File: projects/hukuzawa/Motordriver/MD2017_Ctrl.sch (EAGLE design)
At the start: 7 parts, among them IC1 PIC16F648, J1 3X2A, Q1 CERALOCK

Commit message: 回路図製作経過
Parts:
- added D1, D2, D3, D4: Z-DIODE, FP-21T for MITS:Z-DIODE
- added LED1: (no value), FP-21T for MITS:LED5MM
- added R1: (no value), rcl:R-US_R3216W
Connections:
- new net A: IC1.RB5, IC1.RB6, IC1.RB7
- new net N$1: LED1.C, R1.2
- new net N$2: IC1.T0CKI/RA4, R1.1
- net 5V: now also LED1.A
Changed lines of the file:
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@@
 <part name="U$3" library="FH105" deviceset="8PIN" device=""/>
 <part name="J1" library="3M_372xx" deviceset="3X2" device="A"/>
+<part name="D1" library="FP-21T for MITS" deviceset="Z-DIODE" device=""/>
+<part name="D2" library="FP-21T for MITS" deviceset="Z-DIODE" device=""/>
+<part name="D3" library="FP-21T for MITS" deviceset="Z-DIODE" device=""/>
+<part name="D4" library="FP-21T for MITS" deviceset="Z-DIODE" device=""/>
+<part name="LED1" library="FP-21T for MITS" deviceset="LED" device="5MM"/>
+<part name="R1" library="rcl" deviceset="R-US_" device="R3216W"/>
 </parts>
 <sheets>
@@
 <instance part="J1" gate="2-2" x="-76.2" y="33.02"/>
 <instance part="J1" gate="2-3" x="-76.2" y="27.94"/>
+<instance part="D1" gate="1" x="43.18" y="33.02"/>
+<instance part="D2" gate="1" x="58.42" y="33.02"/>
+<instance part="D3" gate="1" x="58.42" y="22.86" rot="R180"/>
+<instance part="D4" gate="1" x="43.18" y="22.86" rot="R180"/>
+<instance part="LED1" gate="G$1" x="-40.64" y="33.02" rot="R270"/>
+<instance part="R1" gate="G$1" x="-50.8" y="27.94" rot="R90"/>
 </instances>
 <busses>
+<bus name="B$1">
+<segment>
+<wire x1="-66.04" y1="10.16" x2="-66.04" y2="20.32" width="0.762" layer="92"/>
+<wire x1="-66.04" y1="20.32" x2="-55.88" y2="20.32" width="0.762" layer="92"/>
+<wire x1="-55.88" y1="20.32" x2="-55.88" y2="-5.08" width="0.762" layer="92"/>
+<wire x1="-55.88" y1="-5.08" x2="-73.66" y2="-5.08" width="0.762" layer="92"/>
+<wire x1="-73.66" y1="-5.08" x2="-73.66" y2="-22.86" width="0.762" layer="92"/>
+</segment>
+</bus>
 </busses>
 <nets>
@@
 <pinref part="IC1" gate="G$1" pin="VDD"/>
 <wire x1="-63.5" y1="38.1" x2="-35.56" y2="38.1" width="0.1524" layer="91"/>
-<wire x1="-35.56" y1="38.1" x2="-35.56" y2="15.24" width="0.1524" layer="91"/>
+<wire x1="-35.56" y1="38.1" x2="-35.56" y2="33.02" width="0.1524" layer="91"/>
 <label x="-58.42" y="38.608" size="1.778" layer="95"/>
+<pinref part="LED1" gate="G$1" pin="A"/>
+<wire x1="-35.56" y1="33.02" x2="-35.56" y2="15.24" width="0.1524" layer="91"/>
+<wire x1="-38.1" y1="33.02" x2="-35.56" y2="33.02" width="0.1524" layer="91"/>
 </segment>
 </net>
@@
 </segment>
 </net>
+<net name="N$1" class="0">
+<segment>
+<pinref part="R1" gate="G$1" pin="2"/>
+<pinref part="LED1" gate="G$1" pin="C"/>
+<wire x1="-50.8" y1="33.02" x2="-45.72" y2="33.02" width="0.1524" layer="91"/>
+</segment>
+</net>
+<net name="N$2" class="0">
+<segment>
+<pinref part="IC1" gate="G$1" pin="T0CKI/RA4"/>
+<pinref part="R1" gate="G$1" pin="1"/>
+<wire x1="-60.96" y1="-7.62" x2="-50.8" y2="-7.62" width="0.1524" layer="91"/>
+<wire x1="-50.8" y1="-7.62" x2="-50.8" y2="22.86" width="0.1524" layer="91"/>
+</segment>
+</net>
+<net name="A" class="0">
+<segment>
+<pinref part="IC1" gate="G$1" pin="RB7"/>
+<wire x1="-60.96" y1="15.24" x2="-66.04" y2="15.24" width="0.1524" layer="91"/>
+</segment>
+<segment>
+<pinref part="IC1" gate="G$1" pin="RB6"/>
+<wire x1="-60.96" y1="12.7" x2="-66.04" y2="12.7" width="0.1524" layer="91"/>
+</segment>
+<segment>
+<pinref part="IC1" gate="G$1" pin="RB5"/>
+<wire x1="-60.96" y1="10.16" x2="-66.04" y2="10.16" width="0.1524" layer="91"/>
+</segment>
+</net>

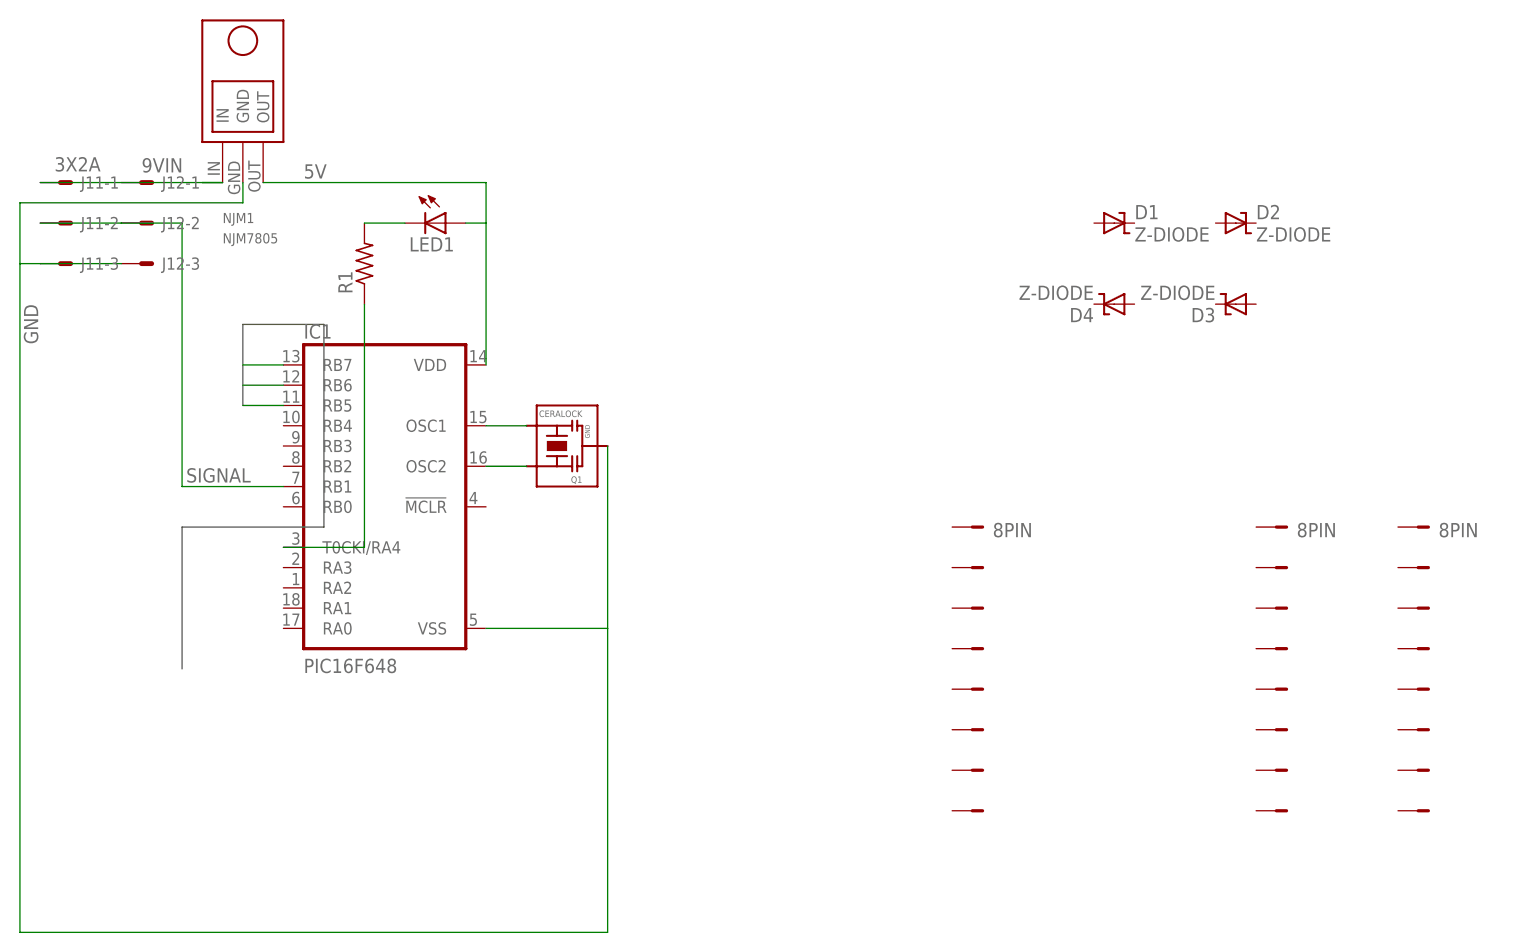
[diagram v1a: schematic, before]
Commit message: 回路図製作経過
制御部配線が7割程度完了
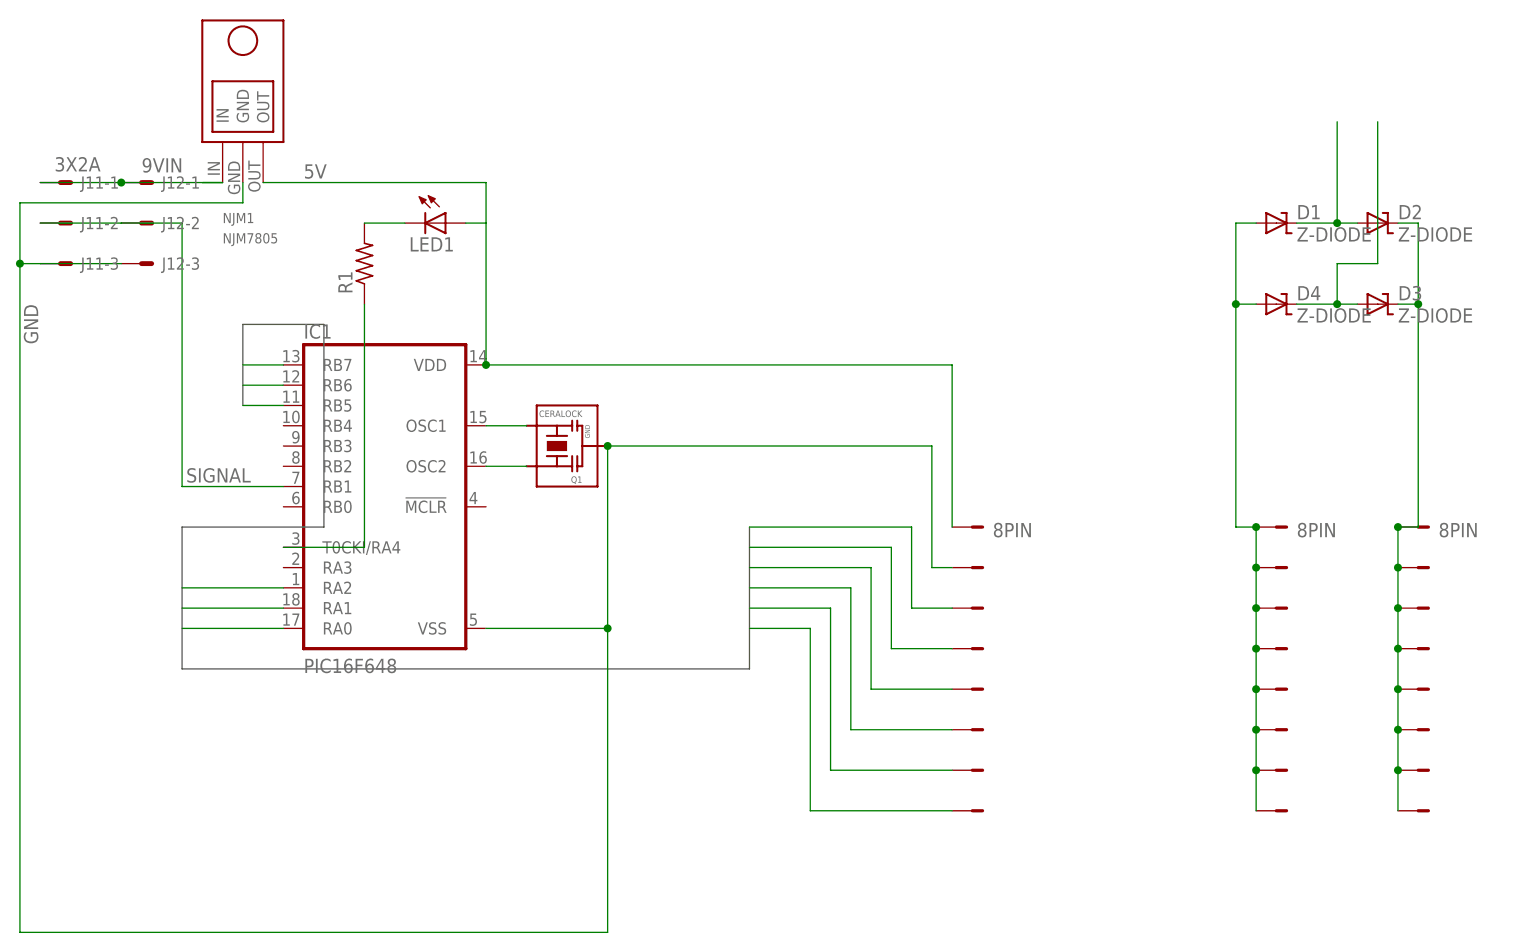
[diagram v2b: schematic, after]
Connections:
- removed net A: IC1.RB5, IC1.RB6, IC1.RB7
- new net AD/B: IC1.RB7, U$1-4.P$1
- new net ADIR: IC1.RB6, U$1-5.P$1
- new net APWM: IC1.RB5, U$1-3.P$1
- new net BD/B: IC1.RA1, U$1-7.P$1
- new net BDIR: IC1.RA2, U$1-8.P$1
- new net BPWM: IC1.RA0, U$1-6.P$1
- new net N$3: D1.A, D4.A, U$2-1.P$1, U$2-2.P$1, U$2-3.P$1, U$2-4.P$1, U$2-5.P$1, U$2-6.P$1, U$2-7.P$1, U$2-8.P$1
- new net N$5: D1.C, D2.A
- new net N$6: D3.A, D4.C
- new net N$7: D2.C, D3.C, U$3-1.P$1, U$3-2.P$1, U$3-3.P$1, U$3-4.P$1, U$3-5.P$1, U$3-6.P$1, U$3-7.P$1, U$3-8.P$1
- net 5V: now also U$1-1.P$1
- net 9VIN: now also J12-1.S
- net GND: now also U$1-2.P$1
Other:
- moved on the sheet: D1, D2, D3, D4

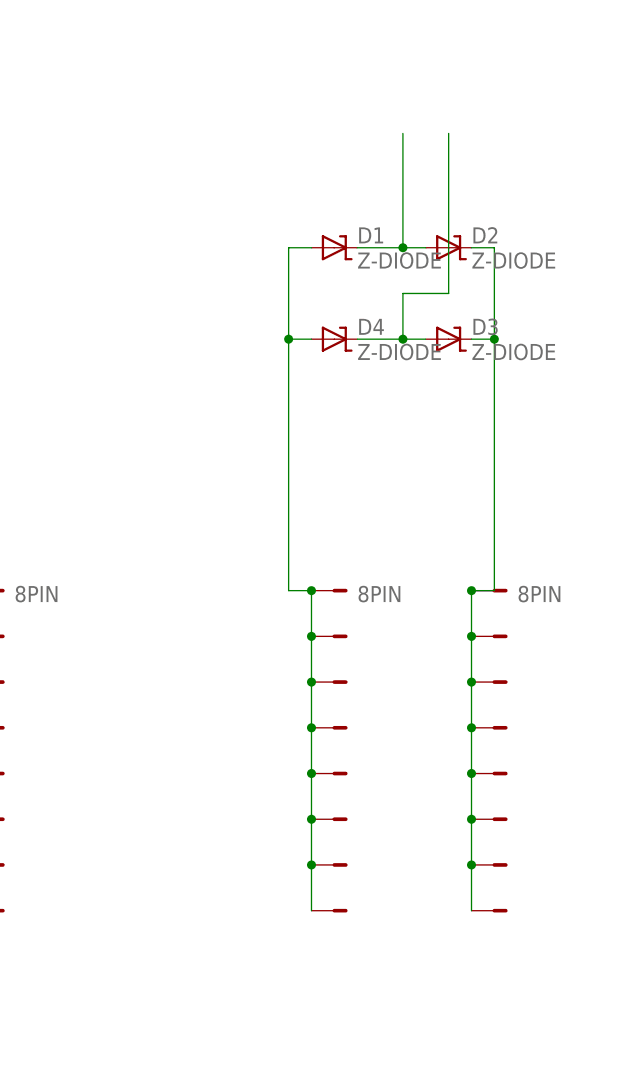
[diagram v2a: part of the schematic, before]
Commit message: モータードライバ制御部回路図製作途中
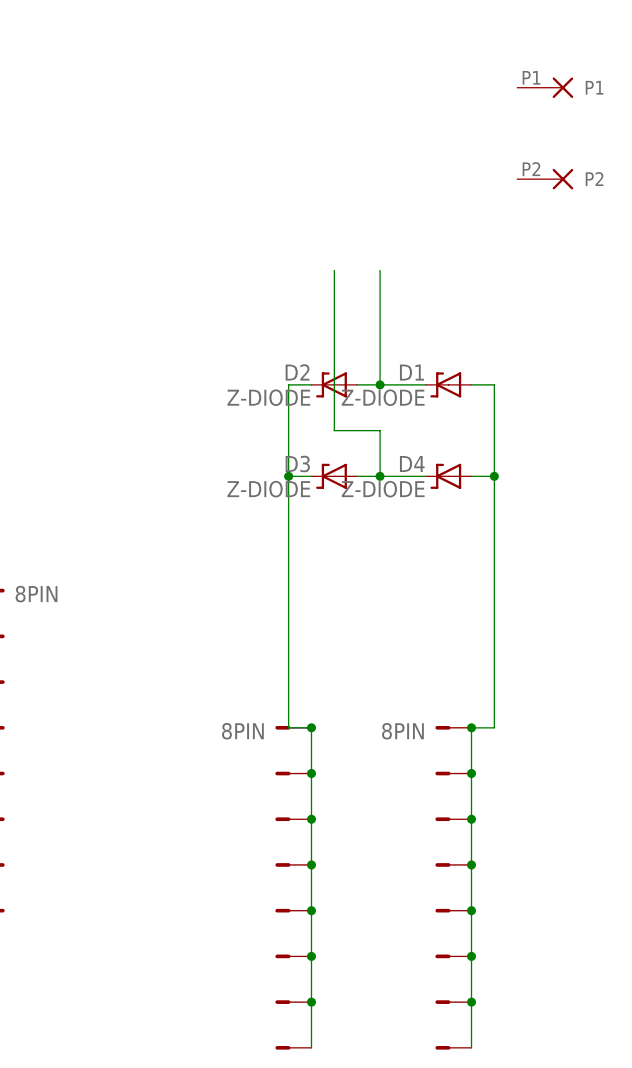
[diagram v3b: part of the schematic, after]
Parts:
- removed U$3: 8PIN, FH105:8PIN
- added POWERNPORT, POWERPPORT: 8PIN, FH105:8PIN
- U$2: value 8PIN -> 2P; device FH105:8PIN -> Powerio:2P
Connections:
- net N$3: now also POWERNPORT-1.P$1, POWERNPORT-2.P$1, POWERNPORT-3.P$1, POWERNPORT-4.P$1, POWERNPORT-5.P$1, POWERNPORT-6.P$1, POWERNPORT-7.P$1, POWERNPORT-8.P$1; no longer U$2-1.P$1, U$2-2.P$1, U$2-3.P$1, U$2-4.P$1, U$2-5.P$1, U$2-6.P$1, U$2-7.P$1, U$2-8.P$1
- net N$7: now also POWERPPORT-1.P$1, POWERPPORT-2.P$1, POWERPPORT-3.P$1, POWERPPORT-4.P$1, POWERPPORT-5.P$1, POWERPPORT-6.P$1, POWERPPORT-7.P$1, POWERPPORT-8.P$1; no longer U$3-1.P$1, U$3-2.P$1, U$3-3.P$1, U$3-4.P$1, U$3-5.P$1, U$3-6.P$1, U$3-7.P$1, U$3-8.P$1
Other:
- moved on the sheet: D1, D2, D3, D4
